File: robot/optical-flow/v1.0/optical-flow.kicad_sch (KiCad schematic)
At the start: 84 parts, among them J1 Conn_ARM_JTAG_SWD_10, J2 SM07B-SRSS-TB, J3 SM07B-SRSS-TB, J4 SM07B-SRSS-TB, J5 BM09B-SRSS-TB, J6 SM06B-SRSS-TB, J7 SM06B-SRSS-TB, J8 SM05B-SRSS-TB, J9 0.1" Header, P1 USB_C_Plug_USB2.0, Q1 BSS138K, SW1 BTN0, SW2 SW_DIP_x04, SW3 RST, U1 STM32F407VETx, Y1 TAXM8M4RDBCCT2T, Y2 Q13FC13500005

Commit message: Schematic feedback
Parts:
- removed JP1: Disable Micro, AT-BoardFeatures:SolderJumper-2_2.0x1.2mm_Open, symbol Jumper:SolderJumper_2_Open
- removed R12: 10k, Resistor_SMD:R_0402_1005Metric, symbol Device:R_Small_US
- added C19, C21: 10u, symbol Device:C_Polarized
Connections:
- net +3.3V: now also C19.1
- net +5V: now also C21.1
- net GND: now also C19.2, C21.2
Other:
- note added: "Display Connector (Designed for use with the 4D Systems uLCD-144G2 LCD Breakout Board)"
- note added: "STM32 has calibrated internal pull-up to sequence"
- note added: "Upstream Power Input"
- note removed: "Display Connector (Designed for use with the 4D Systems uLCD-144G2 LCD Display Module)"
- note removed: "stm32 has calibrated internal pull-up to sequence"
- moved on the sheet: C4, J2, J3, J4, J8, J9, P1, R14, R29, R30, RV1

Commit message: WIP Layout
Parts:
- removed C19: 10u, symbol Device:C_Polarized
- removed D6: XL-1608UOC-06, AT-LED:LED0603, symbol Device:LED
- removed H4: M3, MountingHole:MountingHole_3.2mm_M3, symbol Mechanical:MountingHole
- removed J3: SM07B-SRSS-TB, symbol Connector_Generic_MountingPin:Conn_01x07_MountingPin
- removed J6, J7: SM06B-SRSS-TB, symbol Connector_Generic_MountingPin:Conn_01x06_MountingPin
- removed JP2, JP3: 8MHZ_CLK_LOCAL, AT-BoardFeatures:SolderJumper-2_2.0x1.2mm_Closed, symbol Jumper:SolderJumper_2_Bridged
- removed JP4, JP5: 32KHZ_CLK_LOCAL, AT-BoardFeatures:SolderJumper-2_2.0x1.2mm_Closed, symbol Jumper:SolderJumper_2_Bridged
- removed P1: USB_C_Plug_USB2.0, Connector_USB:USB_C_Receptacle_Molex_105450-0101, symbol Connector:USB_C_Plug_USB2.0
- removed R14: 5.1k, Resistor_SMD:R_0402_1005Metric, symbol Device:R_US
- removed R17, R18, R23, R24: 2.2k, Resistor_SMD:R_0402_1005Metric, symbol Device:R_Small_US
- removed R22, R25, R26, R27, R28: 10k, Resistor_SMD:R_0402_1005Metric, symbol Device:R_Small_US
- added C11: 100u, Capacitor_SMD:CP_Elec_6.3x5.4_Nichicon, symbol Device:C_Polarized_Small_US
- added R23: 100k, Resistor_SMD:R_0402_1005Metric, symbol Device:R_US
- C9: renamed from C21; value 10u -> 100u; footprint (none) -> Capacitor_SMD:CP_Elec_6.3x5.4_Nichicon; symbol Device:C_Polarized -> Device:C_Polarized_Small_US
- J2: renamed from J5; footprint Connector_JST:JST_SH_BM09B-SRSS-TB_1x09-1MP_P1.00mm_Vertical -> Connector_JST:JST_SH_SM09B-SRSS-TB_1x09-1MP_P1.00mm_Horizontal
- J4: renamed from J2; footprint (none) -> Connector_JST:JST_SH_SM07B-SRSS-TB_1x07-1MP_P1.00mm_Horizontal
- J5: renamed from J8; footprint (none) -> Connector_JST:JST_SH_SM05B-SRSS-TB_1x05-1MP_P1.00mm_Horizontal
- J6: renamed from J4; footprint (none) -> Connector_JST:JST_SH_SM07B-SRSS-TB_1x07-1MP_P1.00mm_Horizontal
- SW2: footprint at-switches:CHP-041TB -> AT-Switches:CHP-041TB
- renumbered C9 to C10, C10 to C12, C11 to C13, C12 to C14, C13 to C15, C14 to C16, C15 to C17, C16 to C18, C17 to C19, C4 to C2, C18 to C20, C2 to C3, C3 to C4, D2 to D1, D3 to D2, D4 to D3, D5 to D4, H3 to H2, H2 to H3, J9 to J3, R9 to R10, R31 to R11, R10 to R12, R11 to R13, R29 to R14, R30 to R15, R13 to R16, R15 to R17, R19 to R18, R32 to R19, R33 to R21, R21 to R22, R16 to R6, R6 to R7, R7 to R8, R8 to R9
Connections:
- net OPTICAL_3_INT is gone; now on net OPTICAL_2_INT: J6.6 (Pin_6), U1.81 (PD0)
- net OPTICAL_3_MISO is gone; now on net OPTICAL_2_MISO: J6.5 (Pin_5), U1.79 (PC11)
- net OPTICAL_3_MOSI is gone; now on net OPTICAL_2_MOSI: J6.4 (Pin_4), U1.80 (PC12)
- net OPTICAL_3_NSS is gone; now on net OPTICAL_2_NSS: J6.2 (Pin_2), U1.77 (PA15)
- net OPTICAL_3_SCK is gone; now on net OPTICAL_2_SCK: J6.3 (Pin_3), U1.78 (PC10)
- net +3.3V: now also C11.1, R23.1
- net 32KHZ_CLK_REF: now also C20.1, Y2.2
- net DISPLAY_RX: now also R23.2
- net GND: now also C11.2
- net OPTICAL_2_INT: no longer U1.53 (PB14)
- net OPTICAL_2_MISO: no longer U1.17 (PC2)
- net OPTICAL_2_MOSI: no longer U1.18 (PC3)
- net OPTICAL_2_NSS: no longer U1.51 (PB12)
- net OPTICAL_2_SCK: no longer U1.52 (PB13)
- net at U1.9 (PC15): now also C19.1, Y2.1
- net at C4.1, Y1.3: now also U1.13 (PH1)
- net at C3.1, Y1.1: now also U1.12 (PH0)
- net SHUTDOWN_INITIATED: no longer names the net of U1.88 (PD7)
- net TOF_1_SCL: no longer names the net of U1.92 (PB6)
- net TOF_1_SDA: no longer names the net of U1.93 (PB7)
- net TOF_1_~{INT}: no longer names the net of U1.91 (PB5)
- net TOF_1_~{SHDN}: no longer names the net of U1.90 (PB4)
- net TOF_2_SCL: no longer names the net of U1.47 (PB10)
- net TOF_2_SDA: no longer names the net of U1.48 (PB11)
- net TOF_2_~{INT}: no longer names the net of U1.46 (PE15)
- net TOF_2_~{SHDN}: no longer names the net of U1.45 (PE14)
- net USB_OTG_FS_D_N: no longer names the net of U1.70 (PA11)
- net USB_OTG_FS_D_P: no longer names the net of U1.71 (PA12)
- no-connect marks 32 -> 46
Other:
- note removed: "Optical Flow Connectors (Designed for use with the ST VL53L4CD / SATEL-VL53L4CD Breakout board)"
- note removed: "Standard I2C pull-ups. May need to adjust pull-ups based on measured bus capacitance. Should desolder pull-ups on the SATEL-VL53.. breakout board if these are present."
- note removed: "USB Connection"
- note removed: "~{SHDN} (XSHUT on chip) and ~{INT} (GPIO1 on chip) are Open-drain. On the breakout board, pull-ups are present. Need to populate resistors if using chip directly."
- moved on the sheet: J4, J5, J6

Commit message: Finish switch to G0 and larger space
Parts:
- removed C13, C15, C17, C18: 100n 6.3V, Capacitor_SMD:C_0402_1005Metric, symbol Device:C
- removed C14: 100n, Capacitor_SMD:C_0402_1005Metric, symbol Device:C
- removed C16: 1u, Capacitor_SMD:C_0402_1005Metric, symbol Device:C
- removed C19, C20: 15pF 6.3V, Capacitor_SMD:C_0402_1005Metric, symbol Device:C_Small
- removed C3: 11pF 6.3V, Capacitor_SMD:C_0402_1005Metric, symbol Device:C_Small
- removed C6, C8: 4.7u 6.3V, Capacitor_SMD:C_0402_1005Metric, symbol Device:C
- removed L1: 650 @100MHz, Resistor_SMD:R_0603_1608Metric, symbol Device:L_Ferrite
- removed R10, R7, R8, R9: 10k, Resistor_SMD:R_0402_1005Metric, symbol Device:R_Small_US
- removed R16: 10k, Resistor_SMD:R_0402_1005Metric, symbol Device:R_US
- removed R2, R3, R4, R5: 330, Resistor_SMD:R_0402_1005Metric, symbol Device:R_Small_US
- removed U1: STM32F407VETx, Package_QFP:LQFP-100_14x14mm_P0.5mm, symbol MCU_ST_STM32F4:STM32F407VETx
- added C1, C2: 11pF 6.3V, Capacitor_SMD:C_0402_1005Metric, symbol Device:C_Small
- added C5: 15pF 6.3V, Capacitor_SMD:C_0402_1005Metric, symbol Device:C_Small
- added R10: 100k, Resistor_SMD:R_0402_1005Metric, symbol Device:R_US
- added R11, R12, R13, R22: 330, Resistor_SMD:R_0402_1005Metric, symbol Device:R_Small_US
- added R14, R15, R16: 10k, Resistor_SMD:R_0402_1005Metric, symbol Device:R_Small_US
- added U1: STM32G071RBTx, Package_QFP:LQFP-64_10x10mm_P0.5mm, symbol MCU_ST_STM32G0:STM32G071RBTx
- C10: renamed from C7; value 4.7u 6.3V -> 1u 6.3V
- C3: renamed from C1; value 100n -> 100n 6.3V
- C4: value 11pF 6.3V -> 15pF 6.3V
- renumbered C10 to C11, C9 to C6, C11 to C7, C2 to C8, C5 to C9, H3 to H2, H2 to H3, J3 to J1, J1 to J2, J4 to J3, J6 to J4, J2 to J6, R17 to R1, R14 to R17, R15 to R18, R6 to R19, R18 to R2, R11 to R20, R13 to R21, R20 to R3, R22 to R4, R19 to R5, R21 to R6, R12 to R7, R1 to R8, R23 to R9
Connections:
- net +3.3V: now also U1.6 (VBAT), U1.7 (VREF+), U1.8 (VDD); no longer SW2.5
- net 32KHZ_CLK_REF: now also C4.1, U1.4 (PC14)
- net DIP_0: now also R13.2, U1.47 (PA15)
- net DIP_1: now also R12.2, U1.48 (PC8)
- net DIP_2: now also R11.2, U1.49 (PC9)
- net DISPLAY_RX: now also U1.56 (PD6)
- net DISPLAY_TX: now also U1.55 (PD5)
- net DISPLAY_~{RST}: now also U1.54 (PD4)
- net GND: now also C1.2, C2.2, C5.2, R10.1, R14.1, R15.1, R16.1, U1.9 (VSS)
- net LED_BLUE_1: now also U1.27 (PB0)
- net LED_BLUE_2: now also U1.30 (PB10)
- net LED_GREEN: now also U1.28 (PB1)
- net LED_RED: now also U1.29 (PB2)
- net MCU_BOOT_BOOT0: now also R10.2, R22.1
- net MCU_BOOT_RX: now also U1.1 (PC11)
- net MCU_BOOT_TX: now also U1.64 (PC10)
- net NRST: now also U1.12 (PF2)
- net OPTICAL_1_INT: now also U1.25 (PC4)
- net OPTICAL_1_MISO: now also U1.23 (PA6)
- net OPTICAL_1_MOSI: now also U1.24 (PA7)
- net OPTICAL_1_NSS: now also U1.21 (PA4)
- net OPTICAL_1_SCK: now also U1.22 (PA5)
- net OPTICAL_2_INT: now also U1.37 (PA9/UCPD1_DBCC1)
- net OPTICAL_2_MISO: now also U1.34 (PB14)
- net OPTICAL_2_MOSI: now also U1.35 (PB15)
- net OPTICAL_2_NSS: now also U1.36 (PA8)
- net OPTICAL_2_SCK: now also U1.33 (PB13)
- net SWCLK: now also SW2.4, U1.46 (PA14)
- net SWDIO: now also U1.45 (PA13)
- net USER_ADJ1: now also U1.18 (PA1)
- net USR_BTN: now also U1.51 (PD1)
- net at SW2.2: now also R12.1, R15.2
- net at Y1.3: now also C2.1, U1.11 (PF1); no longer C4.1
- net at SW2.3: now also R13.1, R16.2
- net at SW2.1: now also R11.1, R14.2
- net at Y1.1: now also C1.1, U1.10 (PF0)
- net at Y2.1: now also C5.1, U1.5 (PC15)
- net GPIO_PD10 renamed GPIO_PB5
- net GPIO_PB5: now also U1.59 (PB5)
- net GPIO_PD11 renamed GPIO_PB4
- net GPIO_PB4: now also U1.58 (PB4)
- net GPIO_PD12 renamed GPIO_PB3
- net GPIO_PB3: now also U1.57 (PB3)
- net GPIO_PD9 renamed GPIO_PB6
- net GPIO_PB6: now also U1.60 (PB6)
- net I2C_3_SCL renamed I2C_1_SCL
- net I2C_1_SCL: now also U1.62 (PB8)
- net I2C_3_SDA renamed I2C_1_SDA
- net I2C_1_SDA: now also U1.61 (PB7)
- new net: R22.2, SW2.5
- no-connect marks 46 -> 25
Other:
- note added: "BOOT0 pin shares with SWCLK on G071xx. Refer to DIP Switch section."
- moved on the sheet: RV1, SW2

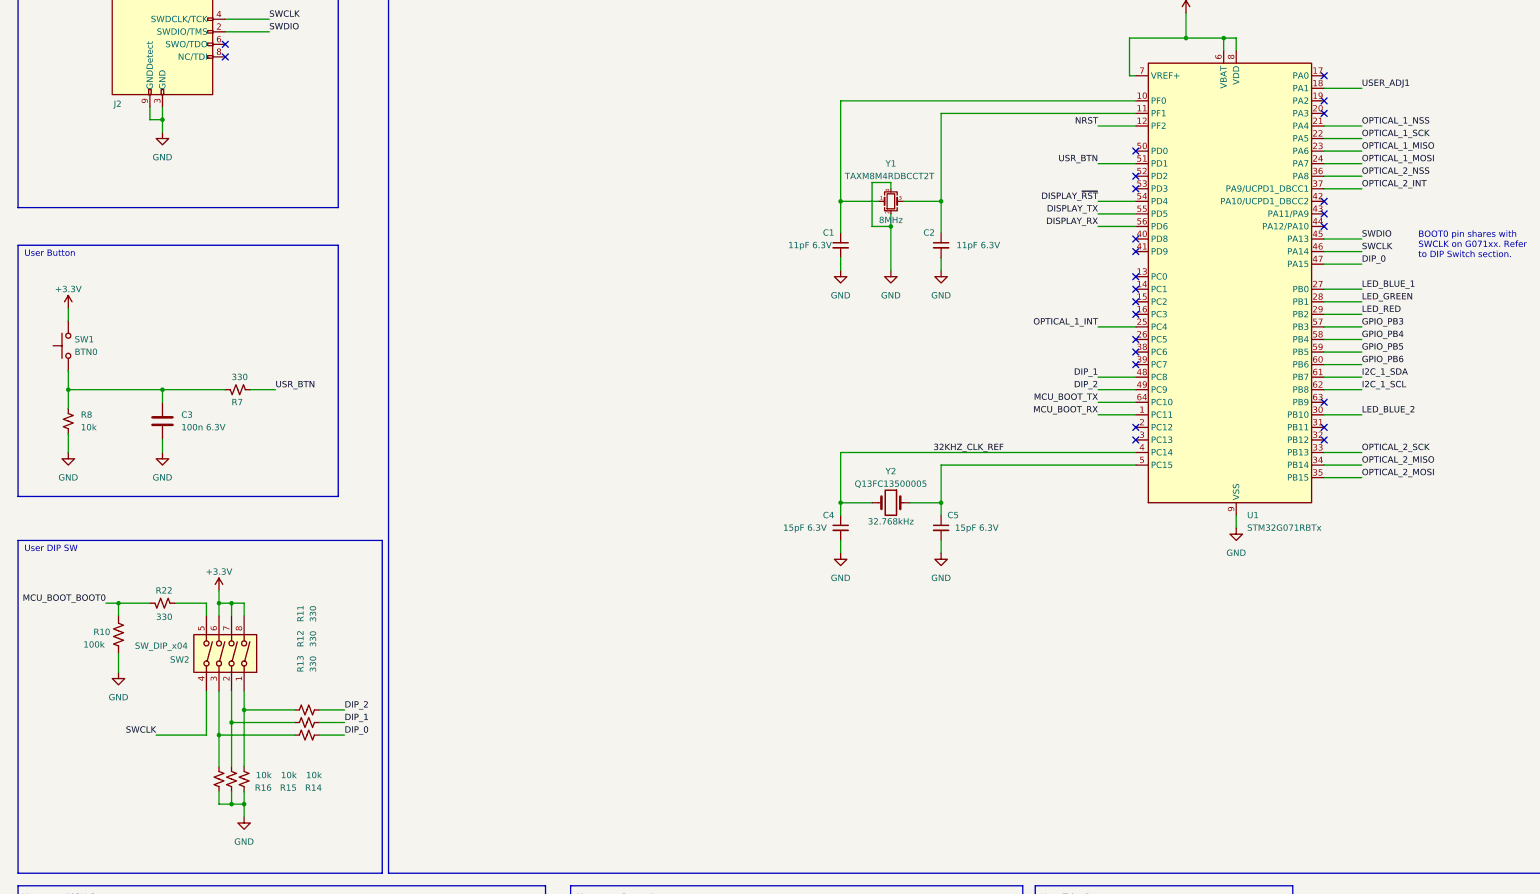
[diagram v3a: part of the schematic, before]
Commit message: Optical flow routing
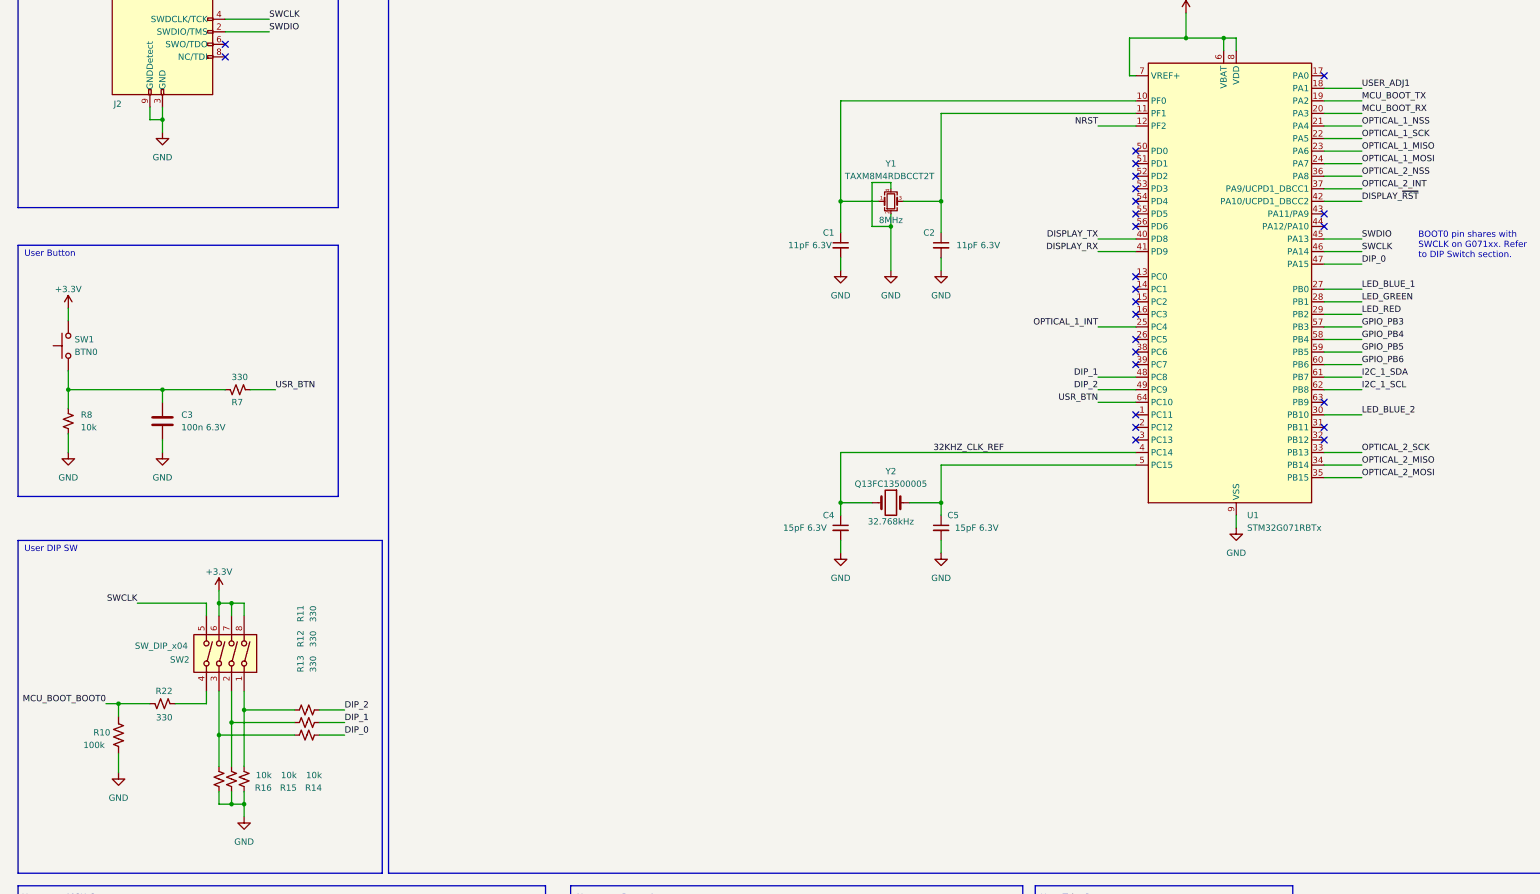
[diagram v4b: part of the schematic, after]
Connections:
- net DISPLAY_RX: now also U1.41 (PD9); no longer U1.56 (PD6)
- net DISPLAY_TX: now also U1.40 (PD8); no longer U1.55 (PD5)
- net DISPLAY_~{RST}: now also U1.42 (PA10/UCPD1_DBCC2); no longer U1.54 (PD4)
- net MCU_BOOT_RX: now also U1.20 (PA3); no longer U1.1 (PC11)
- net MCU_BOOT_TX: now also U1.19 (PA2); no longer U1.64 (PC10)
- net SWCLK: now also SW2.5; no longer SW2.4
- net USR_BTN: now also U1.64 (PC10); no longer U1.51 (PD1)
- net at R22.2: now also SW2.4; no longer SW2.5
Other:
- moved on the sheet: R10, R22

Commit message: Submitted JLCPCB order
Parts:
- J2: footprint AT-Connectors:Samtec-2x5pin-0.5mm -> AT-Connectors:Samtec-2x5pin-1.27mm
- J6: value BM09B-SRSS-TB -> SM09B-SRSS-TB
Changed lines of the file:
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@@
 			)
 		)
-		(property "Value" "BM09B-SRSS-TB"
+		(property "Value" "SM09B-SRSS-TB"
 			(at 62.23 299.72 90)
 			(effects
@@
 			)
 		)
-		(property "Footprint" "AT-Connectors:Samtec-2x5pin-0.5mm"
+		(property "Footprint" "AT-Connectors:Samtec-2x5pin-1.27mm"
 			(at 46.99 97.79 0)
 			(effects
